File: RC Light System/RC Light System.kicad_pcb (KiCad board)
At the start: 2 copper layers, 41.3 x 54 mm, 41 parts, among them J1 INPUT, J10 EX_B, J2 CHAIN, J3 FL_A, J4 FL_B, J5 BR_A, J6 BR_B, J7 BL_L, J8 BL_R, J9 EX_A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

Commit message: First layout done
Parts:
- removed C1: 100nF, Capacitor_THT:C_Disc_D4.7mm_W2.5mm_P5.00mm
- removed JP2: BR_LINK, solder_bridge:bridge_open
- removed JP3: BL_LINK, solder_bridge:bridge_open
- removed JP4: EX_LINK, solder_bridge:bridge_open
- removed Q1, Q2, Q3, Q4, Q5, Q6, Q7, Q8: 2N2222, Package_TO_SOT_THT:TO-92_HandSolder
- removed R10, R12: 180, resistor:R_Axial_DIN0207_L6.3mm_D2.5mm_P7.62mm_Horizontal
- removed R11, R13, R15, R3, R5, R7, R9: 4k7, resistor:R_Axial_DIN0207_L6.3mm_D2.5mm_P7.62mm_Horizontal
- removed R14, R16: 10, resistor:R_Axial_DIN0207_L6.3mm_D2.5mm_P7.62mm_Horizontal
- removed R4: 51, resistor:R_Axial_DIN0207_L6.3mm_D2.5mm_P7.62mm_Horizontal
- removed R6, R8: 200, resistor:R_Axial_DIN0207_L6.3mm_D2.5mm_P7.62mm_Horizontal
- removed RN1: 10k, Resistor_THT:R_Array_SIP9
- removed U1: 74HC595, Package_DIP:DIP-16_W7.62mm_Socket_LongPads
- added A1: Arduino Pro Micro, arduino_pro_micro:Arduino_Pro_Micro, F.Cu at (81.3, 104.8)
- added D1: 1N5819, Diode_THT:D_DO-41_SOD81_P10.16mm_Horizontal, F.Cu at (75.6, 83.2)
- J1: value INPUT -> OUTPUT 1
- J10: value EX_B -> BIND_IN; footprint Connector_JST:JST_XH_B2B-XH-A_1x02_P2.50mm_Vertical -> Connector_PinSocket_2.54mm:PinSocket_1x03_P2.54mm_Vertical; moved to B.Cu
- J2: value CHAIN -> OUTPUT 2
- J3: value FL_A -> STR_IN; footprint Connector_JST:JST_XH_B2B-XH-A_1x02_P2.50mm_Vertical -> Connector_PinSocket_2.54mm:PinSocket_1x03_P2.54mm_Vertical; moved to B.Cu
- J4: value FL_B -> STR_OUT; footprint Connector_JST:JST_XH_B2B-XH-A_1x02_P2.50mm_Vertical -> Connector_PinHeader_2.54mm:PinHeader_1x03_P2.54mm_Vertical
- J5: value BR_A -> THR_IN; footprint Connector_JST:JST_XH_B2B-XH-A_1x02_P2.50mm_Vertical -> Connector_PinSocket_2.54mm:PinSocket_1x03_P2.54mm_Vertical; moved to B.Cu
- J6: value BR_B -> THR_OUT; footprint Connector_JST:JST_XH_B2B-XH-A_1x02_P2.50mm_Vertical -> Connector_PinHeader_2.54mm:PinHeader_1x03_P2.54mm_Vertical
- J7: value BL_L -> AUX_IN; footprint Connector_JST:JST_XH_B2B-XH-A_1x02_P2.50mm_Vertical -> Connector_PinSocket_2.54mm:PinSocket_1x03_P2.54mm_Vertical; moved to B.Cu
- J8: value BL_R -> AUX_OUT; footprint Connector_JST:JST_XH_B2B-XH-A_1x02_P2.50mm_Vertical -> Connector_PinHeader_2.54mm:PinHeader_1x03_P2.54mm_Vertical
- J9: value EX_A -> VBATT; footprint Connector_JST:JST_XH_B2B-XH-A_1x02_P2.50mm_Vertical -> rc_light_system:Conn_Light_Power
- JP1: value FL_LINK -> BIND; footprint solder_bridge:bridge_open -> Connector_PinHeader_2.54mm:PinHeader_1x02_P2.54mm_Vertical; moved to F.Cu
- R1: value 4k7 -> 470
- R2: value 51 -> 560
- moved JP1 46.4 mm to (65.4, 121.3)
- moved R1 45.7 mm to (71.8, 86.4), turned to 0 degrees
- moved R2 40.8 mm to (82.5, 86.4)
- moved J3 33.9 mm to (81.3, 118.7), turned to 0 degrees
- moved J5 27.8 mm to (78.7, 118.7), turned to 0 degrees
- moved J10 26.5 mm to (76.2, 118.7), turned to 0 degrees
- moved J9 25.0 mm to (94.6, 84.5), turned to 90 degrees
- moved J7 18.8 mm to (83.8, 118.7), turned to 0 degrees
- moved J8 13.6 mm to (94.6, 113.7), turned to 0 degrees
- moved J6 11.4 mm to (94.6, 103.5), turned to 0 degrees
- moved J4 9.44 mm to (94.6, 93.3), turned to 0 degrees
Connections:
- J1 pad 5: /SER_CLK -> /SER_CLK_1
- J10 pad 1: Net-(J10-Pad1) -> GND
- J10 pad 2: VCC -> (no net)
- J2 pad 4: Net-(J2-Pad4) -> /SER_DATA
- J2 pad 5: /SER_CLK -> /SER_CLK_2
- J3 pad 1: Net-(J3-Pad1) -> GND
- J3 pad 2: VCC -> /BEC
- J4 pad 1: Net-(J4-Pad1) -> GND
- J4 pad 2: VCC -> /BEC
- J5 pad 1: Net-(J5-Pad1) -> GND
- J5 pad 2: VCC -> /BEC
- J6 pad 1: Net-(J6-Pad1) -> GND
- J6 pad 2: VCC -> /BEC
- J7 pad 1: Net-(J7-Pad1) -> GND
- J7 pad 2: VCC -> /BEC
- J8 pad 1: Net-(J8-Pad1) -> GND
- J8 pad 2: VCC -> /BEC
- J9 pad 2: VCC -> GND
- JP1 pad 1: Net-(J4-Pad1) -> GND
- JP1 pad 2: Net-(J3-Pad1) -> Net-(J10-Pad3)
- R1 pad 1: Net-(Q1-Pad2) -> VCC
- R1 pad 2: FL_A -> Net-(A1-Pad20)
- R2 pad 1: Net-(Q1-Pad1) -> Net-(A1-Pad20)
- R2 pad 2: Net-(J3-Pad1) -> GND
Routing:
- net VCC: track 160.5 -> 65.9 mm
- net FL_A: track 73.8 -> 0.00 mm
- net Net-(J4-Pad1): track 64.2 -> 0.00 mm, vias 1 -> 0
- net Net-(J3-Pad1): track 62.2 -> 0.00 mm
- net FL_B: track 60.0 -> 0.00 mm
- net Net-(J8-Pad1): track 59.1 -> 0.00 mm
- net /BEC: track 0.00 -> 54.5 mm
- net BR_A: track 52.7 -> 0.00 mm
- net BR_B: track 47.2 -> 0.00 mm
- net Net-(J6-Pad1): track 44.4 -> 0.00 mm, vias 1 -> 0
- net /SER_CLK: track 44.1 -> 0.00 mm, vias 1 -> 0
- net Net-(J5-Pad1): track 42.7 -> 0.00 mm
- net /AUX: track 0.00 -> 39.6 mm
- net Net-(J7-Pad1): track 36.7 -> 0.00 mm
- net +5V: track 67.7 -> 32.0 mm, vias 1 -> 0
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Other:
- board size 41.3 x 54 mm -> 34.3 x 41.3 mm
- net class BEC added: clearance 0.2, trace_width 0.5, via_dia 0.8, via_drill 0.4
- board text added: "+"
- board text added: "-"
- board text added: "1N 5819"
- board text added: "2S LIPO NIMH"
- board text added: "AUX"
- board text added: "BIND"
- board text added: "OUTPUT 1"
- board text added: "OUTPUT 2"
- board text added: "RC Light System "Big Chief" Rev. A"
- board text added: "STR"
- board text added: "THR"
- board text removed: "BL_L"
- board text removed: "BL_R"
- board text removed: "BR_A"
- board text removed: "BR_B"
- board text removed: "EX_A"
- board text removed: "EX_B"
- board text removed: "FL_A"
- board text removed: "FL_B"
- board text removed: "RC Light System Output "Big Boy" Rev. A"

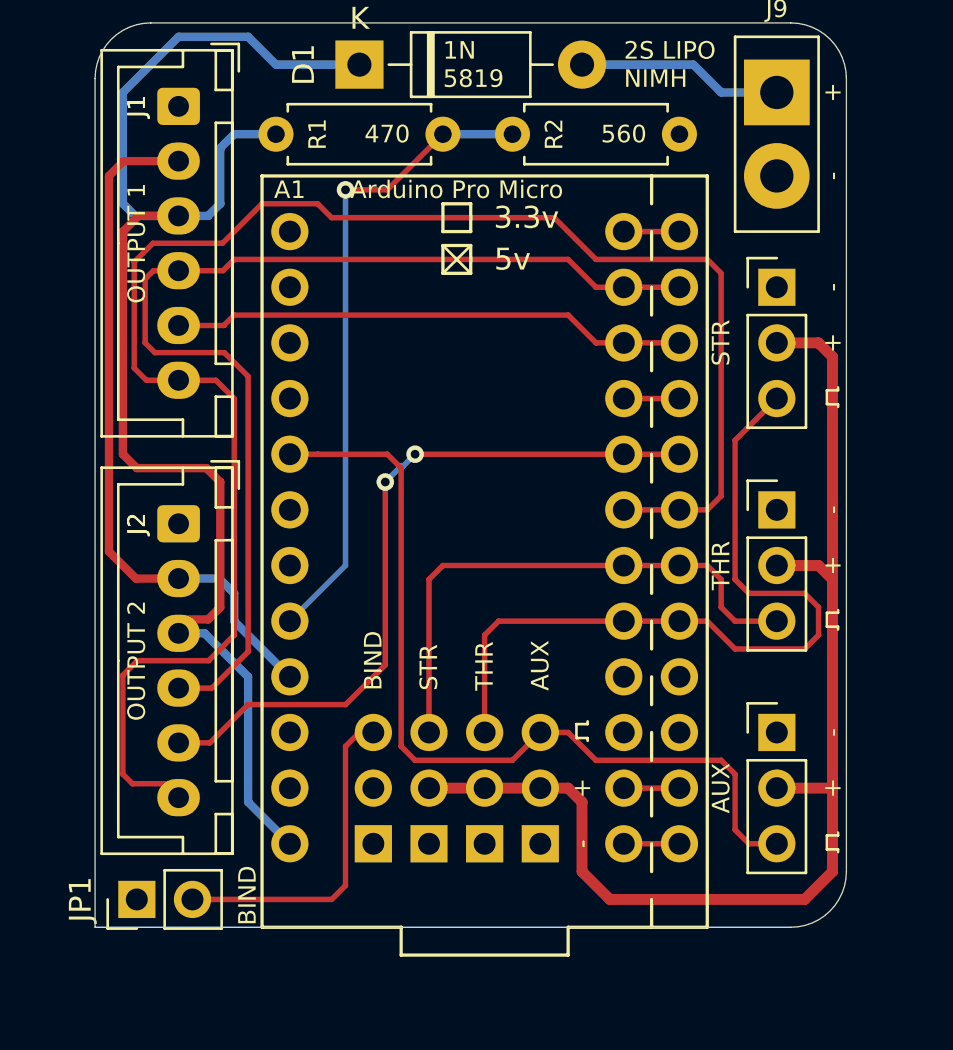
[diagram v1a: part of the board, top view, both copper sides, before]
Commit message: Added voltage dividers
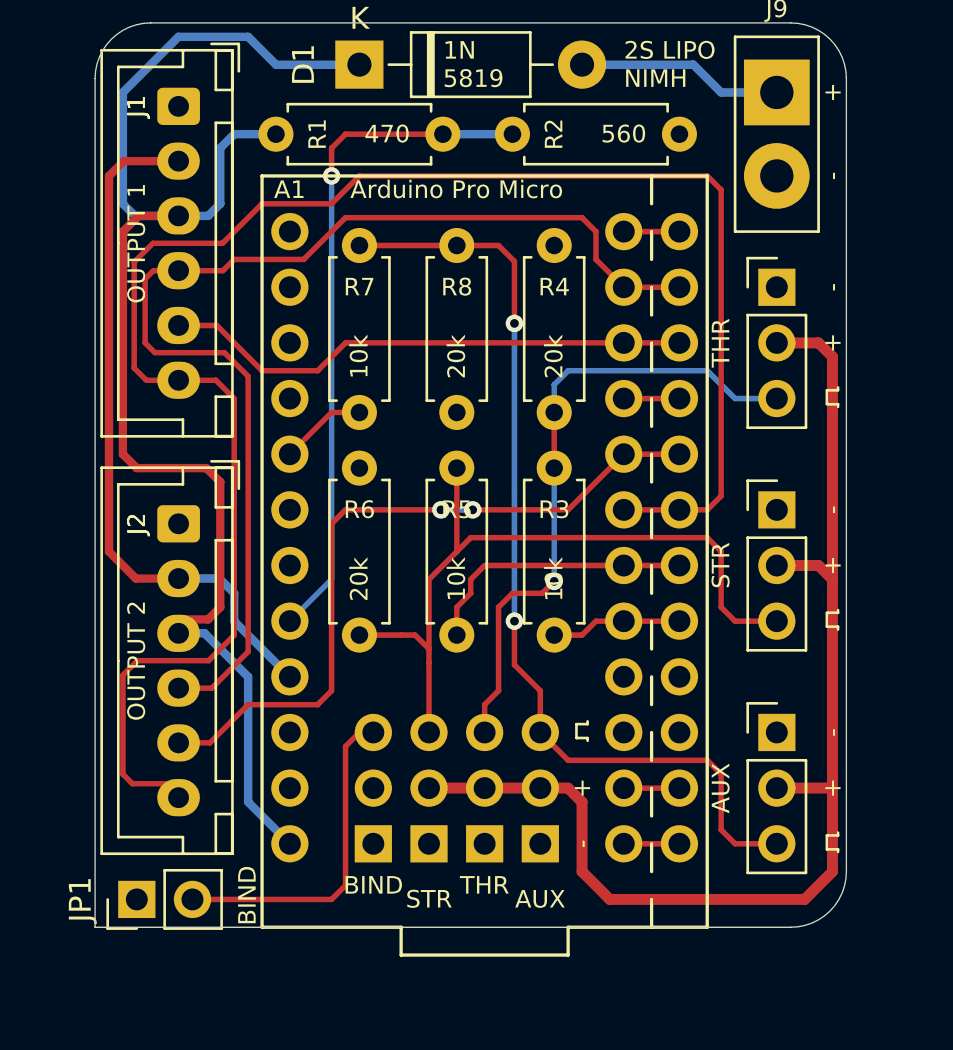
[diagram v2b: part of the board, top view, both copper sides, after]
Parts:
- added R3: 10k, resistor:R_Axial_DIN0207_L6.3mm_D2.5mm_P7.62mm_Horizontal, F.Cu at (84.5, 109.2)
- added R4: 20k, resistor:R_Axial_DIN0207_L6.3mm_D2.5mm_P7.62mm_Horizontal, F.Cu at (84.5, 99.1)
- added R5: 10k, resistor:R_Axial_DIN0207_L6.3mm_D2.5mm_P7.62mm_Horizontal, F.Cu at (80.0, 109.2)
- added R6: 20k, resistor:R_Axial_DIN0207_L6.3mm_D2.5mm_P7.62mm_Horizontal, F.Cu at (75.6, 109.2)
- added R7: 10k, resistor:R_Axial_DIN0207_L6.3mm_D2.5mm_P7.62mm_Horizontal, F.Cu at (75.6, 99.1)
- added R8: 20k, resistor:R_Axial_DIN0207_L6.3mm_D2.5mm_P7.62mm_Horizontal, F.Cu at (80.0, 91.4)
- J3: value STR_IN -> THR_IN
- J4: value STR_OUT -> THR_OUT
- J5: value THR_IN -> STR_IN
- J6: value THR_OUT -> STR_OUT
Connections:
- A1 pad 17: /AUX -> AUX
- A1 pad 5: /THR -> THR
- A1 pad 6: /STR -> STR
- J3 pad 3: /THR -> Net-(J3-Pad3)
- J4 pad 3: /THR -> Net-(J3-Pad3)
- J5 pad 3: /STR -> Net-(J5-Pad3)
- J6 pad 3: /STR -> Net-(J5-Pad3)
- J7 pad 3: /AUX -> Net-(J7-Pad3)
- J8 pad 3: /AUX -> Net-(J7-Pad3)
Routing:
- net Net-(J7-Pad3): track 0.00 -> 43.8 mm, vias 0 -> 2
- net /AUX: track 39.6 -> 0.00 mm
- net /THR: track 35.4 -> 0.00 mm
- net Net-(J5-Pad3): track 0.00 -> 34.0 mm
- net Net-(J3-Pad3): track 0.00 -> 28.9 mm, vias 0 -> 1
- net /STR: track 24.9 -> 0.00 mm
- net STR: track 0.00 -> 12.6 mm
- net THR: track 0.00 -> 5.98 mm
- net AUX: track 0.00 -> 3.96 mm
- net /SER_LATCH: track 77.9 -> 81.2 mm
- net /SER_DATA: track 50.0 -> 52.3 mm
- net Net-(A1-Pad20): track 29.4 -> 30.9 mm
- net /SER_CLK_1: track 23.6 -> 24.2 mm
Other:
- board text added: "RC Light System "Big Chief" Rev. B"
- board text removed: "RC Light System "Big Chief" Rev. A"
